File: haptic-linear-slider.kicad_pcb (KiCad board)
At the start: 2 copper layers, 130.5 x 33.8 mm, 56 parts, among them IC1 DIO54335TST6, IC2 TLV61048DBVR, J1 SWD_TagConnect, J2 USB_C_Receptacle_USB2.0_16P, J3 TBC05-02-1-G-G, SW1 SW_Push, SW2 SW_Push, U1 RP2354_60QFN, U2 PSM01-081A-103B2, U3 DRV8876PWPR, Y1 ABM8-272-T3

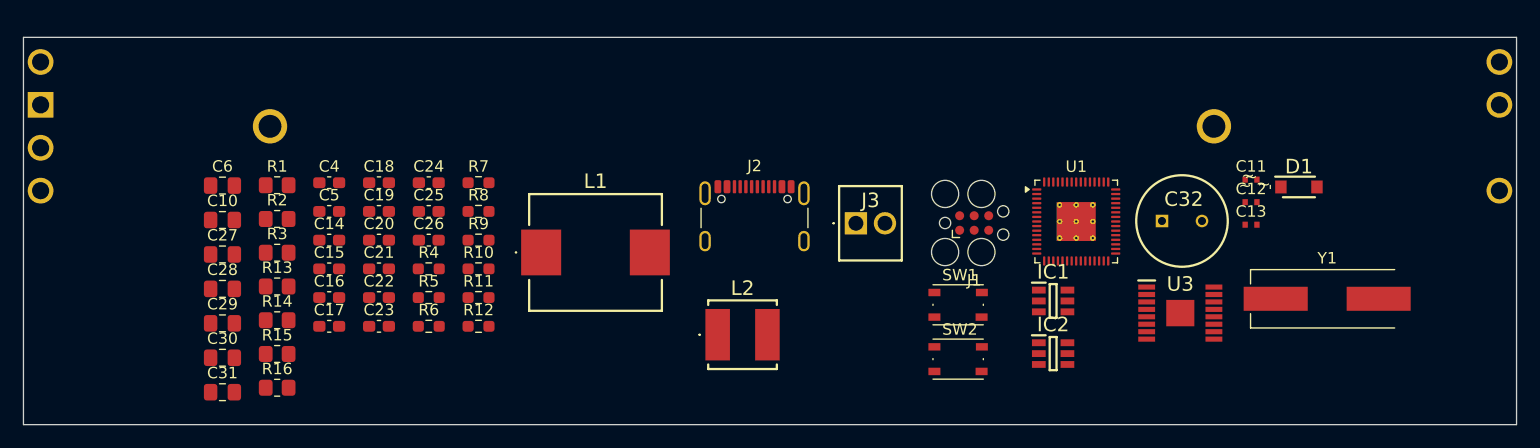
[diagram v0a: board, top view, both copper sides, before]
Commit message: feat: symbols and cleaning, ESD
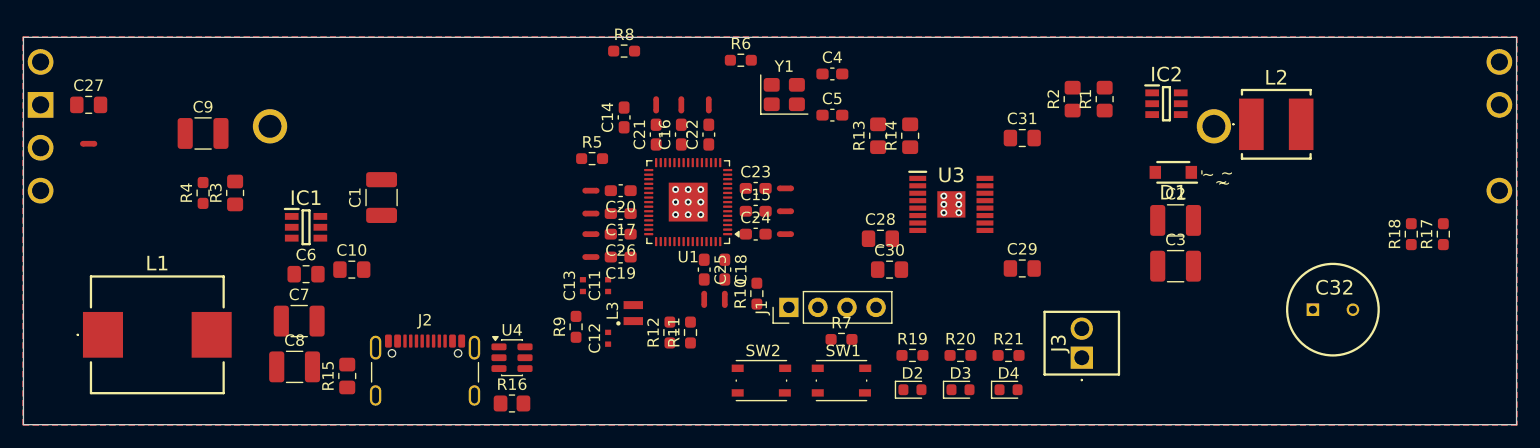
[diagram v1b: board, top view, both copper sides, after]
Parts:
- added C1: 10u, Capacitor_SMD:C_1210_3225Metric_Pad1.33x2.70mm_HandSolder, F.Cu at (241.2, 213.6)
- added C2: 10u, Capacitor_SMD:C_1210_3225Metric_Pad1.33x2.70mm_HandSolder, F.Cu at (310.6, 215.6)
- added C3: 10u, Capacitor_SMD:C_1210_3225Metric_Pad1.33x2.70mm_HandSolder, F.Cu at (310.6, 219.6)
- added C7: 10u, Capacitor_SMD:C_1210_3225Metric_Pad1.33x2.70mm_HandSolder, F.Cu at (234.0, 224.4)
- added C8: 10u, Capacitor_SMD:C_1210_3225Metric_Pad1.33x2.70mm_HandSolder, F.Cu at (233.6, 228.4)
- added C9: 10u, Capacitor_SMD:C_1210_3225Metric_Pad1.33x2.70mm_HandSolder, F.Cu at (225.6, 208.0)
- added D2: Green, LED_SMD:LED_0603_1608Metric, F.Cu at (287.6, 230.4)
- added D3: Green, LED_SMD:LED_0603_1608Metric, F.Cu at (291.8, 230.4)
- added D4: Red, LED_SMD:LED_0603_1608Metric, F.Cu at (296.0, 230.4)
- added L3: 3u3, _Footprints:L_pol_2016, F.Cu at (263.2, 223.7)
- added NT1: NetTie_2, NetTie:NetTie-2_SMD_Pad0.5mm, F.Cu at (276.5, 214.8)
- added NT10: NetTie_2, NetTie:NetTie-2_SMD_Pad0.5mm, F.Cu at (276.5, 216.8)
- added NT11: NetTie_2, NetTie:NetTie-2_SMD_Pad0.5mm, F.Cu at (269.4, 222.5)
- added NT12: NetTie_2, NetTie:NetTie-2_SMD_Pad0.5mm, F.Cu at (259.5, 216.8)
- added NT13: NetTie_2, NetTie:NetTie-2_SMD_Pad0.5mm, F.Cu at (215.6, 208.9)
- added NT2: NetTie_2, NetTie:NetTie-2_SMD_Pad0.5mm, F.Cu at (267.4, 205.5)
- added NT3: NetTie_2, NetTie:NetTie-2_SMD_Pad0.5mm, F.Cu at (259.5, 215.0)
- added NT4: NetTie_2, NetTie:NetTie-2_SMD_Pad0.5mm, F.Cu at (271.2, 222.5)
- added NT5: NetTie_2, NetTie:NetTie-2_SMD_Pad0.5mm, F.Cu at (259.5, 218.8)
- added NT6: NetTie_2, NetTie:NetTie-2_SMD_Pad0.5mm, F.Cu at (259.5, 213.0)
- added NT7: NetTie_2, NetTie:NetTie-2_SMD_Pad0.5mm, F.Cu at (265.2, 205.5)
- added NT8: NetTie_2, NetTie:NetTie-2_SMD_Pad0.5mm, F.Cu at (269.8, 205.5)
- added NT9: NetTie_2, NetTie:NetTie-2_SMD_Pad0.5mm, F.Cu at (276.5, 212.8)
- added R17: 1k, Resistor_SMD:R_0603_1608Metric_Pad0.98x0.95mm_HandSolder, F.Cu at (334.0, 216.8)
- added R18: 1M, Resistor_SMD:R_0603_1608Metric_Pad0.98x0.95mm_HandSolder, F.Cu at (331.2, 216.8)
- added R19: 1k, Resistor_SMD:R_0603_1608Metric_Pad0.98x0.95mm_HandSolder, F.Cu at (287.6, 227.4)
- added R20: 1k, Resistor_SMD:R_0603_1608Metric_Pad0.98x0.95mm_HandSolder, F.Cu at (291.8, 227.4)
- added R21: 1k, Resistor_SMD:R_0603_1608Metric_Pad0.98x0.95mm_HandSolder, F.Cu at (296.0, 227.4)
- added U4: USBLC6-2SC6, Package_TO_SOT_SMD:SOT-23-6, F.Cu at (252.6, 227.6)
- C15: value 4u7 -> 100n
- C16: value 100n -> 4u7
- J1: value SWD_TagConnect -> SWD; footprint Connector:Tag-Connect_TC2030-IDC-FP_2x03_P1.27mm_Vertical -> Connector_PinHeader_2.54mm:PinHeader_1x04_P2.54mm_Vertical
- U1: footprint Package_DFN_QFN:QFN-60-1EP_7x7mm_P0.4mm_EP3.4x3.4mm_ThermalVias -> Package_DFN_QFN:QFN-60-1EP_7x7mm_P0.4mm_EP3.4x3.4mm
- Y1: footprint _Footprints:Crystal_SMD_HC49-US -> Crystal:Crystal_SMD_3225-4Pin_3.2x2.5mm
- moved C31 73.3 mm to (297.2, 208.4)
- moved R1 72.7 mm to (304.4, 205.0), turned to 90 degrees
- moved R2 70.3 mm to (301.6, 205.0), turned to 90 degrees
- moved C29 70.1 mm to (297.2, 219.8)
- moved IC1 65.6 mm to (234.6, 216.2)
- moved C30 58.8 mm to (285.6, 219.9)
- moved C13 58.6 mm to (258.8, 221.3), turned to 90 degrees
- moved C28 57.7 mm to (284.8, 217.2)
- moved R14 57.6 mm to (287.4, 208.2), turned to 90 degrees
- moved C12 57.4 mm to (261.0, 225.9), turned to 90 degrees
- moved C11 57.0 mm to (261.0, 221.3), turned to 90 degrees
- moved R13 54.2 mm to (284.6, 208.2), turned to 90 degrees
- moved Y1 50.7 mm to (276.4, 204.6)
- moved L2 50.1 mm to (319.4, 207.2)
- moved C4 45.0 mm to (280.6, 202.8)
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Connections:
- J1 pad 1: +3V3 -> /SWCLK
- J1 pad 2: /SWD -> GND
- J1 pad 3: Net-(J1-~{RESET}) -> /SWD
- J1 pad 4: /SWCLK -> /SWD_RUN
- R5 pad 1: Net-(J1-~{RESET}) -> /SWD_RUN
- U1 pad 34: unconnected-(U1-GPIO22-Pad34) -> /GPIO22
- U1 pad 36: unconnected-(U1-GPIO24-Pad36) -> /GPIO24
- U1 pad 37: unconnected-(U1-GPIO25-Pad37) -> /GPIO25
- U2 pad 7: unconnected-(U2-T-Pad7) -> /TOUCH
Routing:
- net GND: vias 0 -> 15
- added copper zone on B.Cu, net GND
- added copper zone on F.Cu, net GND
